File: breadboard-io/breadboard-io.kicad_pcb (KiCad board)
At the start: 2 copper layers, 33 x 19.1 mm, 30 parts, among them J1 Conn_01x10_Male, Q1 DMN3300U, Q2 DMN3300U, Q3 DMN3300U, Q4 DMN3300U, SW1 SW0, SW2 SW0, SW3 SW0, SW4 SW0

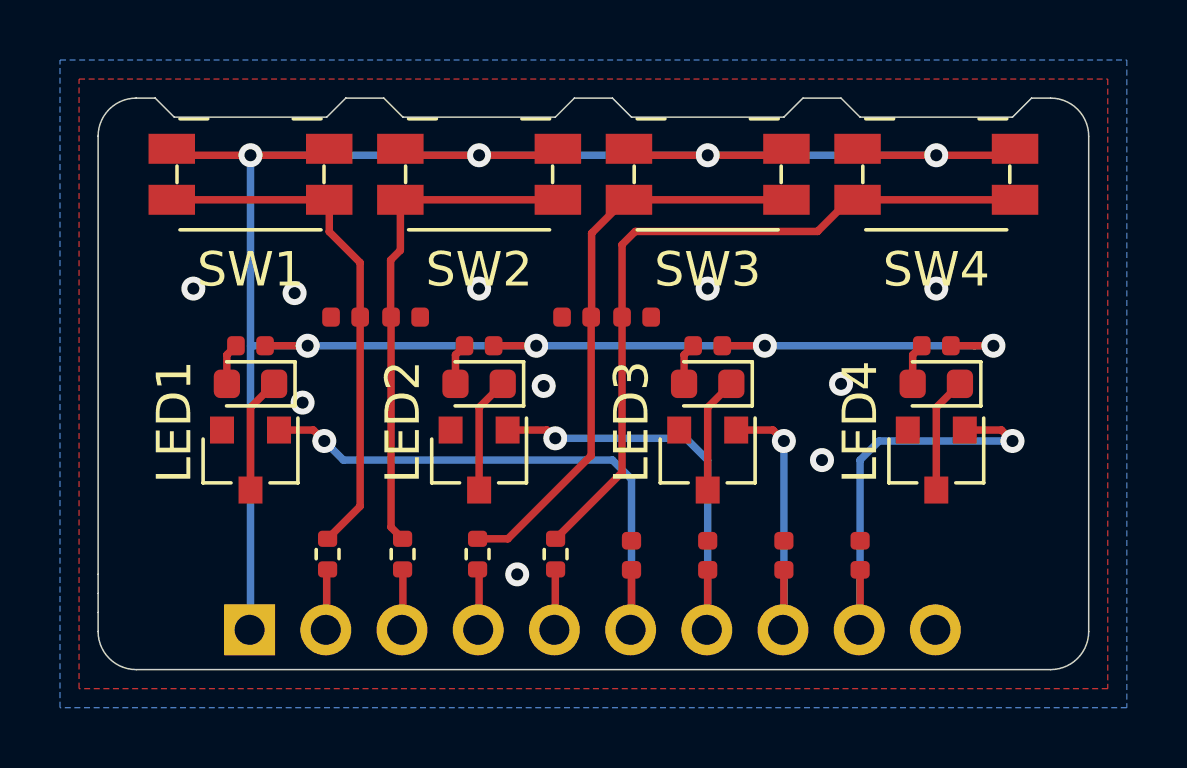
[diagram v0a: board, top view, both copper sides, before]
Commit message: Fixing PCB annotations
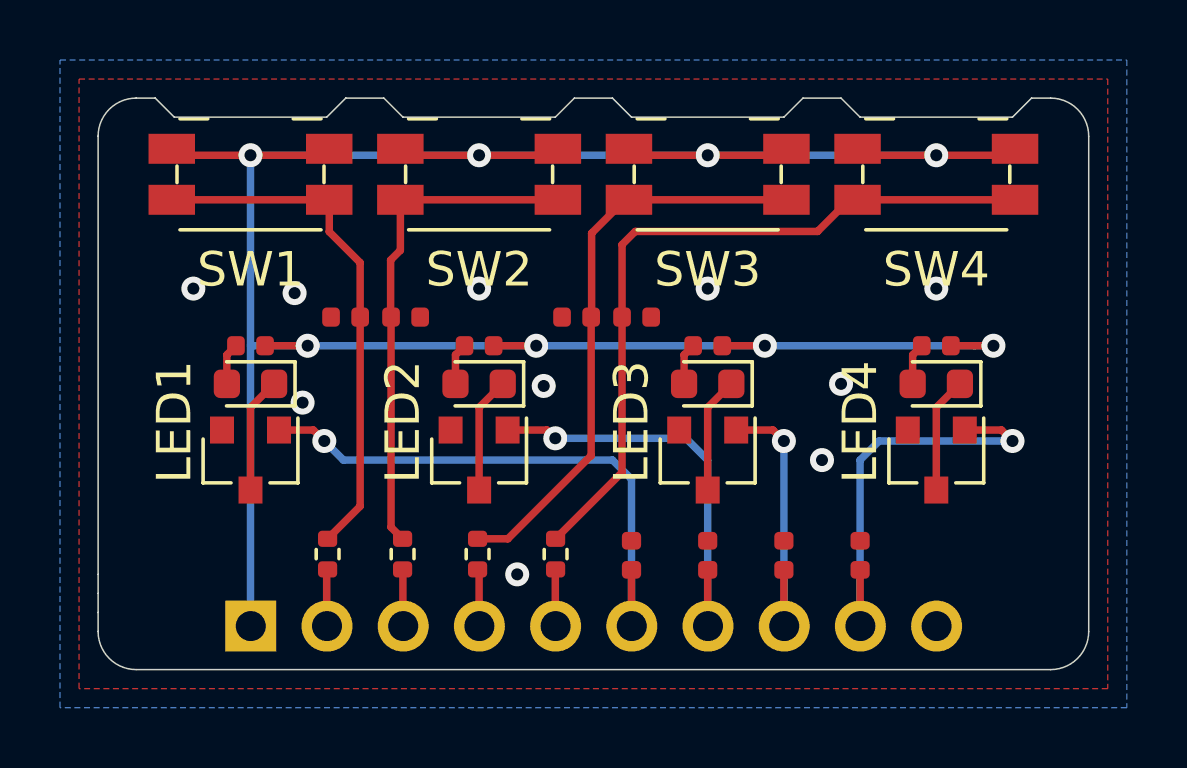
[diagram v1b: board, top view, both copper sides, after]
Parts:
- D1, D2, D3, D4: value LED -> G
- J1: value Conn_01x10_Male -> 68016-410HLF
- Q1, Q2, Q3, Q4: value DMN3300U -> DMN3023L-7
- R13, R14, R15, R16: value 1k -> 10k
- moved J1 0.13 mm to (125.7, 119.2)

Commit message: Added everyday dev logo in silk
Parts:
- removed the G*** at (148.0, 107.6)
- added G***: LOGO, breadboard-io:edd-logo-silk, B.Cu at (148.0, 107.5)
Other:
- board text added: "everday dev"

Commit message: Update logo in silkscreen
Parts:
- removed the G*** at (148.0, 107.5)
- added G***: LOGO, breadboard-io:everydaydev, B.Cu at (137.0, 105.9)
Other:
- board text added: "os.everydaydev.io"
- board text removed: "everday dev"
